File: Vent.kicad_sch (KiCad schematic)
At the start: 4 parts, among them U1 ESP32-S3-WROOM-1, U2 MCP9808T-E_MS

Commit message: USB-to-UART
Original-author: Zachariah K. Sharma <zachariah.sharma@gmail.com>
Source-commit: c72ab2fed98419bb1f096896306b36ff3456098c
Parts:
- added C1: 100nF, PCM_JLCPCB:C_0805, symbol PCM_JLCPCB-Capacitors:0805,100nF
- added C2: 4.7uF, PCM_JLCPCB:C_0805, symbol PCM_JLCPCB-Capacitors:0805,4.7uF
- added J1: TYPE-C-31-M-12, TYPE-C-31-M-12:HRO_TYPE-C-31-M-12, symbol TYPE-C-31-M-12:TYPE-C-31-M-12
- added Q1: S8050 J3Y 200-350, PCM_JLCPCB:Q_SOT-23, symbol PCM_JLCPCB-Transistors:NPN,S8050 J3Y 200-350
- added R3, R4: 5.1kΩ, PCM_JLCPCB:R_0603, symbol PCM_JLCPCB-Resistors:0603,5.1kΩ
- added U3: CP2102N-A02-GQFN28R, CP2102N-A02-GQFN28R:IC_CP2102N-A02-GQFN28R, symbol CP2102N-A02-GQFN28R:CP2102N-A02-GQFN28R
- added U4: AP2112K-3.3TRG1, AP2112K-3.3TRG1:SOT95P285X140-5N, symbol AP2112K-3.3TRG1:AP2112K-3.3TRG1
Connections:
- net +3.3V: now also U4.5 (VOUT)
- net GND: now also C1.2, C2.2, J1.A1_B12 (GND), J1.B1_A12 (GND), J1.S1 (SHIELD), J1.S2 (SHIELD), J1.S3 (SHIELD), J1.S4 (SHIELD), R3.2, R4.1, U3.3 (GND), U4.2 (GND)
- net RXD0: now reaches U1.36 (RXD0)
- net RXD0: now also U3.26 (TXD)
- net TXD0: now reaches U1.37 (TXD0)
- net TXD0: now also U3.25 (RXD)
- new net: C1.1, C2.1, U3.6 (VDD)
- new net: J1.A5 (CC1), R3.1
- new net: J1.B5 (CC2), R4.2
- new net USB_D+: J1.A6 (DP1), J1.B6 (DP2), U3.4 (D+)
- new net USB_D-: J1.A7 (DN1), J1.B7 (DN2), U3.5 (D-)
- new net VBUS: J1.A4_B9 (VBUS), J1.B4_A9 (VBUS), U3.7 (VREGIN), U3.8 (VBUS), U4.1 (VIN)
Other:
- note added: "Autoprogramming Circuit"
- note added: "ESP-32"
- note added: "Temperature Sensor"
- note added: "USB-to-UART"
- moved on the sheet: R1, R2, U1, U2

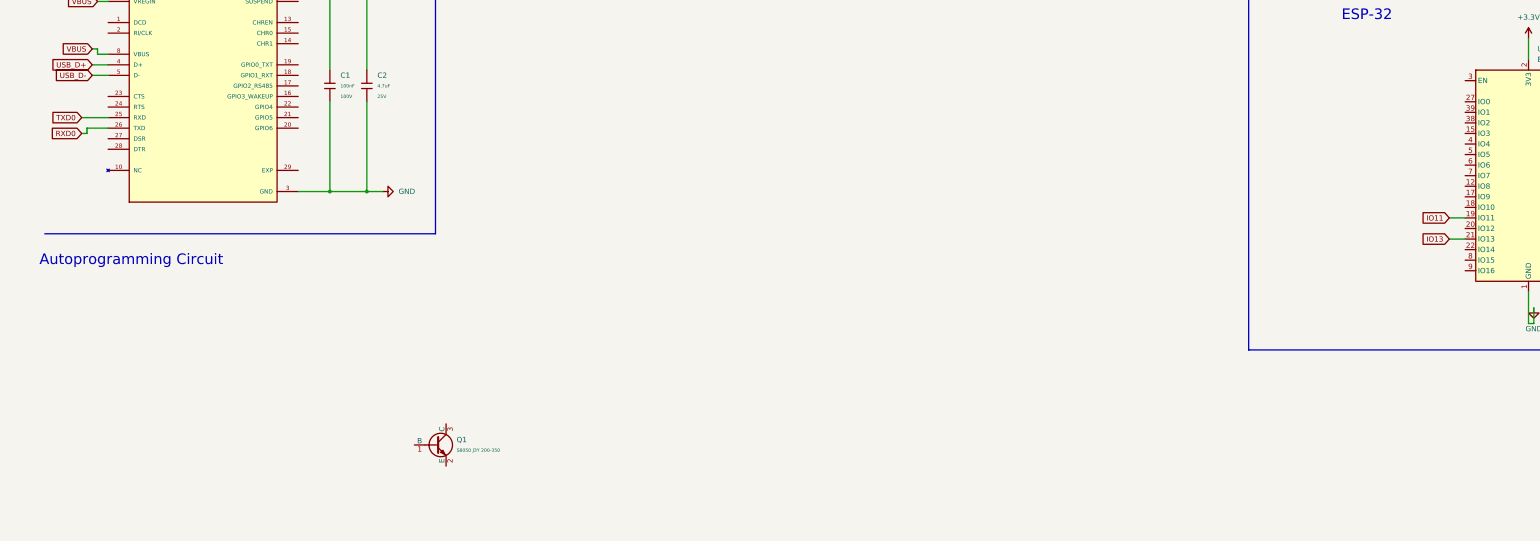
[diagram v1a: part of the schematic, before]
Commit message: Autoprogramming Circuit
Original-author: Zachariah K. Sharma <zachariah.sharma@gmail.com>
Source-commit: 72ef880672316db68a35278d5394047a9c77ba1c
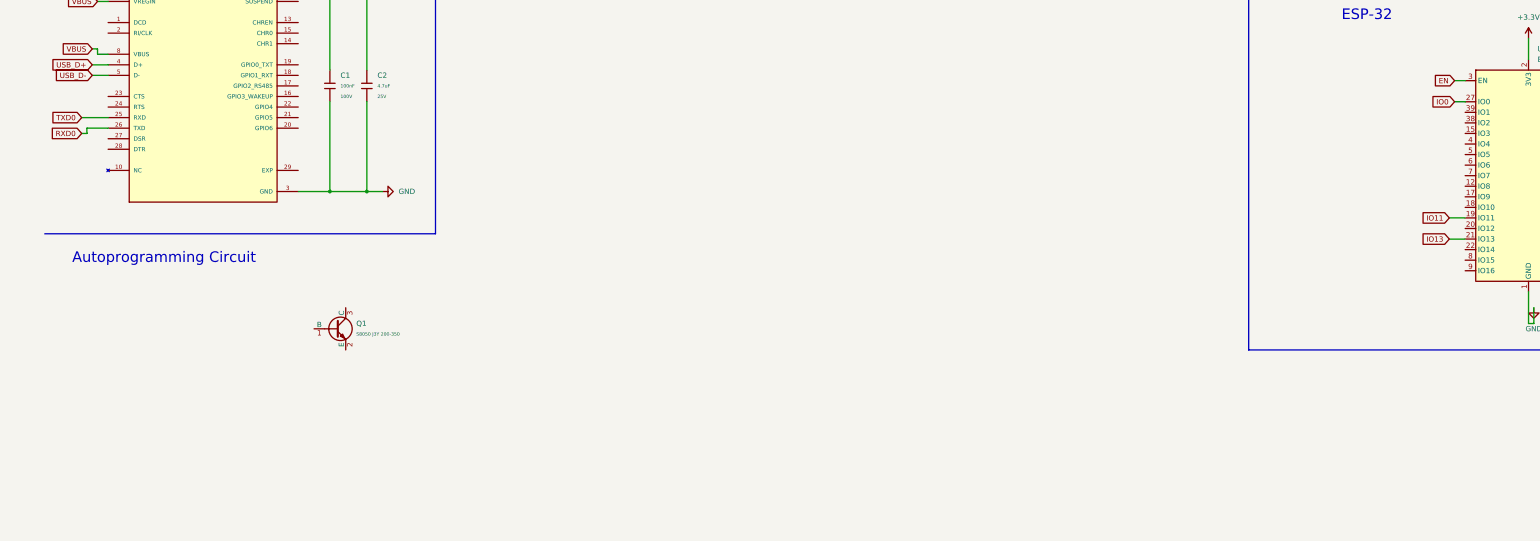
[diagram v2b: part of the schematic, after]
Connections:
- net IO0: now reaches U1.27 (IO0)
- net EN: now reaches U1.3 (EN)
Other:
- moved on the sheet: Q1
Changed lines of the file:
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@@
 	(text "Autoprogramming Circuit"
 		(exclude_from_sim no)
-		(at 36.068 146.05 0)
+		(at 43.942 145.542 0)
 		(effects
 			(font
@@
 	(wire
 		(pts
+			(xy 354.33 102.87) (xy 356.87 102.87)
+		)
+		(stroke
+			(width 0)
+			(type default)
+		)
+	)
+	(wire
+		(pts
 			(xy 72.39 44.45) (xy 73.66 44.45)
 		)
@@
 	(wire
 		(pts
+			(xy 354.33 107.95) (xy 356.87 107.95)
+		)
+		(stroke
+			(width 0)
+			(type default)
+		)
+	)
+	(wire
+		(pts
 			(xy 27.94 83.82) (xy 30.48 83.82)
 		)
@@
 		(property "Intersheetrefs" "${INTERSHEET_REFS}"
 			(at 20.0562 83.82 0)
+			(effects
+				(font
+					(size 1.27 1.27)
+				)
+				(justify right)
+				(hide yes)
+			)
+		)
+	)
+	(global_label "IO0"
+		(shape input)
+		(at 354.33 107.95 180)
+		(fields_autoplaced yes)
+		(effects
+			(font
+				(size 1.27 1.27)
+			)
+			(justify right)
+		)
+		(property "Intersheetrefs" "${INTERSHEET_REFS}"
+			(at 348.2 107.95 0)
+			(effects
+				(font
+					(size 1.27 1.27)
+				)
+				(justify right)
+				(hide yes)
+			)
+		)
+	)
+	(global_label "EN"
+		(shape input)
+		(at 354.33 102.87 180)
+		(fields_autoplaced yes)
+		(effects
+			(font
+				(size 1.27 1.27)
+			)
+			(justify right)
+		)
+		(property "Intersheetrefs" "${INTERSHEET_REFS}"
+			(at 348.8653 102.87 0)
 			(effects
 				(font
@@
 	(symbol
 		(lib_id "PCM_JLCPCB-Transistors:NPN,S8050 J3Y 200-350")
-		(at 109.22 190.5 0)
+		(at 85.09 162.56 0)
 		(unit 1)
 		(exclude_from_sim no)
@@
 		(fields_autoplaced yes)
 		(property "Reference" "Q1"
-			(at 114.3 189.2299 0)
+			(at 90.17 161.2899 0)
 			(effects
 				(font
@@
 		)
 		(property "Value" "S8050 J3Y 200-350"
-			(at 114.3 191.77 0)
+			(at 90.17 163.83 0)
 			(effects
 				(font
@@
 		)
 		(property "Footprint" "PCM_JLCPCB:Q_SOT-23"
-			(at 107.442 190.5 90)
+			(at 83.312 162.56 90)
 			(effects
 				(font
@@
 		)
 		(property "Datasheet" "https://www.lcsc.com/datasheet/lcsc_datasheet_2310131500_Jiangsu-Changjing-Electronics-Technology-Co---Ltd--S8050-J3Y-RANGE-200-350_C2146.pdf"
-			(at 109.22 190.5 0)
+			(at 85.09 162.56 0)
 			(effects
 				(font
@@
 		)
 		(property "Description" "25V 300mW 200@50mA,1V 500mA NPN SOT-23 Bipolar (BJT) ROHS"
-			(at 109.22 190.5 0)
+			(at 85.09 162.56 0)
 			(effects
 				(font
@@
 		)
 		(property "LCSC" "C2146"
-			(at 109.22 190.5 0)
+			(at 85.09 162.56 0)
 			(effects
 				(font
@@
 		)
 		(property "Stock" "1211209"
-			(at 109.22 190.5 0)
+			(at 85.09 162.56 0)
 			(effects
 				(font
@@
 		)
 		(property "Price" "0.017USD"
-			(at 109.22 190.5 0)
+			(at 85.09 162.56 0)
 			(effects
 				(font
@@
 		)
 		(property "Process" "SMT"
-			(at 109.22 190.5 0)
+			(at 85.09 162.56 0)
 			(effects
 				(font
@@
 		)
 		(property "Minimum Qty" "10"
-			(at 109.22 190.5 0)
+			(at 85.09 162.56 0)
 			(effects
 				(font
@@
 		)
 		(property "Attrition Qty" "5"
-			(at 109.22 190.5 0)
+			(at 85.09 162.56 0)
 			(effects
 				(font
@@
 		)
 		(property "Class" "Basic Component"
-			(at 109.22 190.5 0)
+			(at 85.09 162.56 0)
 			(effects
 				(font
@@
 		)
 		(property "Category" "Transistors,Bipolar Transistors - BJT"
-			(at 109.22 190.5 0)
+			(at 85.09 162.56 0)
 			(effects
 				(font
@@
 		)
 		(property "Manufacturer" "Changjiang Electronics Tech (CJ)"
-			(at 109.22 190.5 0)
+			(at 85.09 162.56 0)
 			(effects
 				(font
@@
 		)
 		(property "Part" "S8050 J3Y(RANGE:200-350)"
-			(at 109.22 190.5 0)
+			(at 85.09 162.56 0)
 			(effects
 				(font
@@
 		)
 		(property "Transition Frequency (fT)" "150MHz"
-			(at 109.22 190.5 0)
+			(at 85.09 162.56 0)
 			(effects
 				(font
@@
 		)
 		(property "Operating Temperature" "-55°C~+150°C"
-			(at 109.22 190.5 0)
+			(at 85.09 162.56 0)
 			(effects
 				(font
@@
 		)
 		(property "Collector Cut-Off Current (Icbo)" "100nA"
-			(at 109.22 190.5 0)
+			(at 85.09 162.56 0)
 			(effects
 				(font
@@
 		)
 		(property "Transistor Type" "NPN"
-			(at 109.22 190.5 0)
+			(at 85.09 162.56 0)
 			(effects
 				(font
@@
 		)
 		(property "DC Current Gain (hFE@Ic,Vce)" "200@500mA,1V"
-			(at 109.22 190.5 0)
+			(at 85.09 162.56 0)
 			(effects
 				(font
@@
 		)
 		(property "Power Dissipation (Pd)" "300mW"
-			(at 109.22 190.5 0)
+			(at 85.09 162.56 0)
 			(effects
 				(font
@@
 		)
 		(property "Collector Current (Ic)" "500mA"
-			(at 109.22 190.5 0)
+			(at 85.09 162.56 0)
 			(effects
 				(font
@@
 		)
 		(property "Collector-Emitter Saturation Voltage (VCE(sat)@Ic,Ib)" "600mV@500mA,50mA"
-			(at 109.22 190.5 0)
+			(at 85.09 162.56 0)
 			(effects
 				(font
@@
 		)
 		(property "Collector-Emitter Breakdown Voltage (Vceo)" "25V"
-			(at 109.22 190.5 0)
-			(effects
-				(font
+			(at 85.09 162.56 0)
+			(effects
+				(font

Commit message: Fixed most of the bugs hopefully
Original-author: Zachariah K. Sharma <zachariah.sharma@gmail.com>
Source-commit: 95630e4fc29616ac93e070c71f119a40b19bcd80
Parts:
- added C3, C4: 10uF, PCM_JLCPCB:C_0603, symbol PCM_JLCPCB-Capacitors:0603,10uF
- added C5: 1uF, PCM_JLCPCB:C_0603, symbol PCM_JLCPCB-Capacitors:0603,1uF
- added C6: 100nF, PCM_JLCPCB:C_0805, symbol PCM_JLCPCB-Capacitors:0805,100nF
- added Q2: S8050 J3Y 200-350, PCM_JLCPCB:Q_SOT-23, symbol PCM_JLCPCB-Transistors:NPN,S8050 J3Y 200-350
- added R5, R6, R7, R8: 10kΩ, PCM_JLCPCB:R_0603, symbol PCM_JLCPCB-Resistors:0603,10kΩ
- J1: footprint TYPE-C-31-M-12:HRO_TYPE-C-31-M-12 -> Footprints:HRO_TYPE-C-31-M-12
- U3: footprint CP2102N-A02-GQFN28R:IC_CP2102N-A02-GQFN28R -> Footprints:IC_CP2102N-A02-GQFN28R
- U4: footprint AP2112K-3.3TRG1:SOT95P285X140-5N -> Footprints:SOT95P285X140-5N
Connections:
- net +3.3V: now also C4.1, C5.1, R7.1, R8.1
- net EN: now also Q1.3 (C), C6.1, R7.2
- net GND: now also Q1.2 (E), U2.5 (A2), U2.6 (A1), U2.7 (A0), U3.29 (EXP), C4.2, C5.2, C6.2, Q2.2 (E)
- net IO0: now also Q2.3 (C), R8.2
- net USB_D+: now also U1.14 (USB_D+)
- net USB_D-: now also U1.13 (USB_D-)
- net VBUS: now also C3.1
- net at Q1.1 (B): now also R6.2
- net at U4.3 (EN): now also C3.2
- net RTS: now reaches U3.24 (RTS)
- net RTS: now also R5.1
- net DTR: now reaches U3.28 (DTR)
- net DTR: now also R6.1
- new net: Q2.1 (B), R5.2
- no-connect marks 0 -> 49
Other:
- note added: "Puck"
- note added: "Voltage Regulator"
- company: (none) -> Vynte
- title: (none) -> Vynte Puck
- moved on the sheet: C1, C2, Q1
